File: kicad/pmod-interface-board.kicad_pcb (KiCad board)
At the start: 4 copper layers, 82.9 x 61 mm, 30 parts, among them J1 PMOD Connector 1, J2 PMOD Connector 2, J4 Gameboy Cart Connector, U1 74HCT541, U2 74HCT541, U3 74HC595, U4 74HC595, U5 74HC595, U6 74HC597

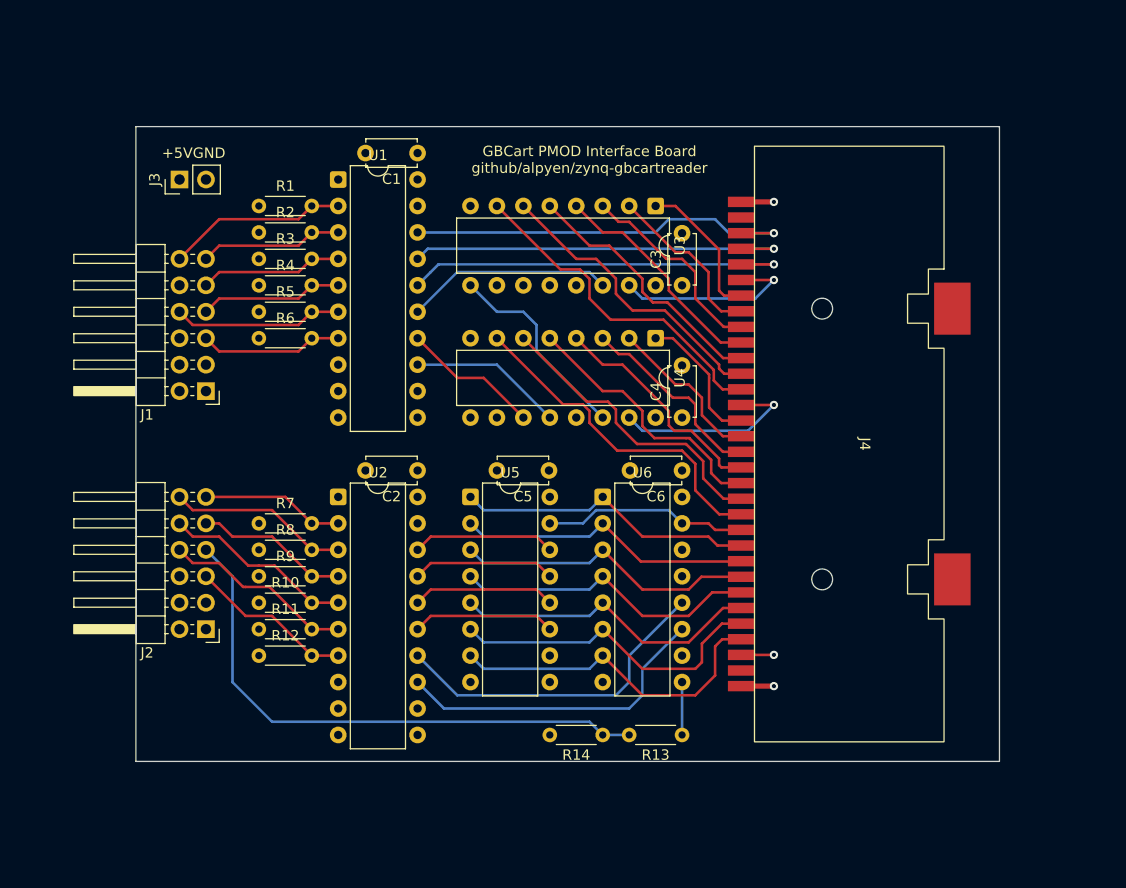
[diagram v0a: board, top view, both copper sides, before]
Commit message: kicad: pcb excess shortened
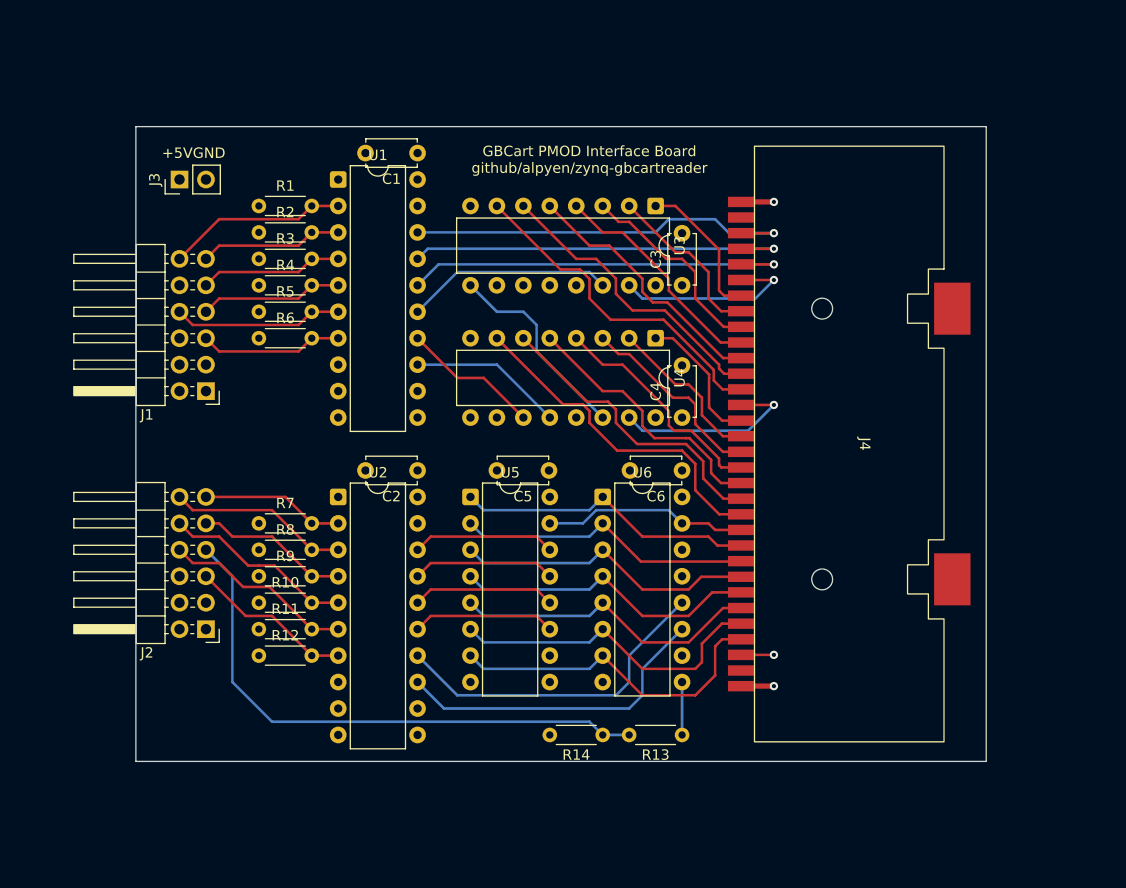
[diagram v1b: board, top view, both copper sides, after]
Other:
- board size 82.9 x 61 mm -> 81.7 x 61 mm
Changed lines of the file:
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@@
 	(gr_rect
 		(start 110.109 60.96)
-		(end 193.04 121.92)
+		(end 191.77 121.92)
 		(stroke
 			(width 0.05)
@@
 	(gr_line
 		(start 96.52 91.44)
-		(end 208.28 91.44)
+		(end 203.2 91.44)
 		(stroke
 			(width 0.15)
@@
 		(polygon
 			(pts
-				(xy 104.14 55.88) (xy 198.12 55.88) (xy 198.12 127) (xy 104.14 127)
+				(xy 104.14 55.88) (xy 196.85 55.88) (xy 196.85 127) (xy 104.14 127)
 			)
 		)
@@
 		(polygon
 			(pts
-				(xy 106.68 58.42) (xy 195.58 58.42) (xy 195.58 124.46) (xy 106.68 124.46)
+				(xy 106.68 58.42) (xy 194.31 58.42) (xy 194.31 124.46) (xy 106.68 124.46)
 			)
 		)

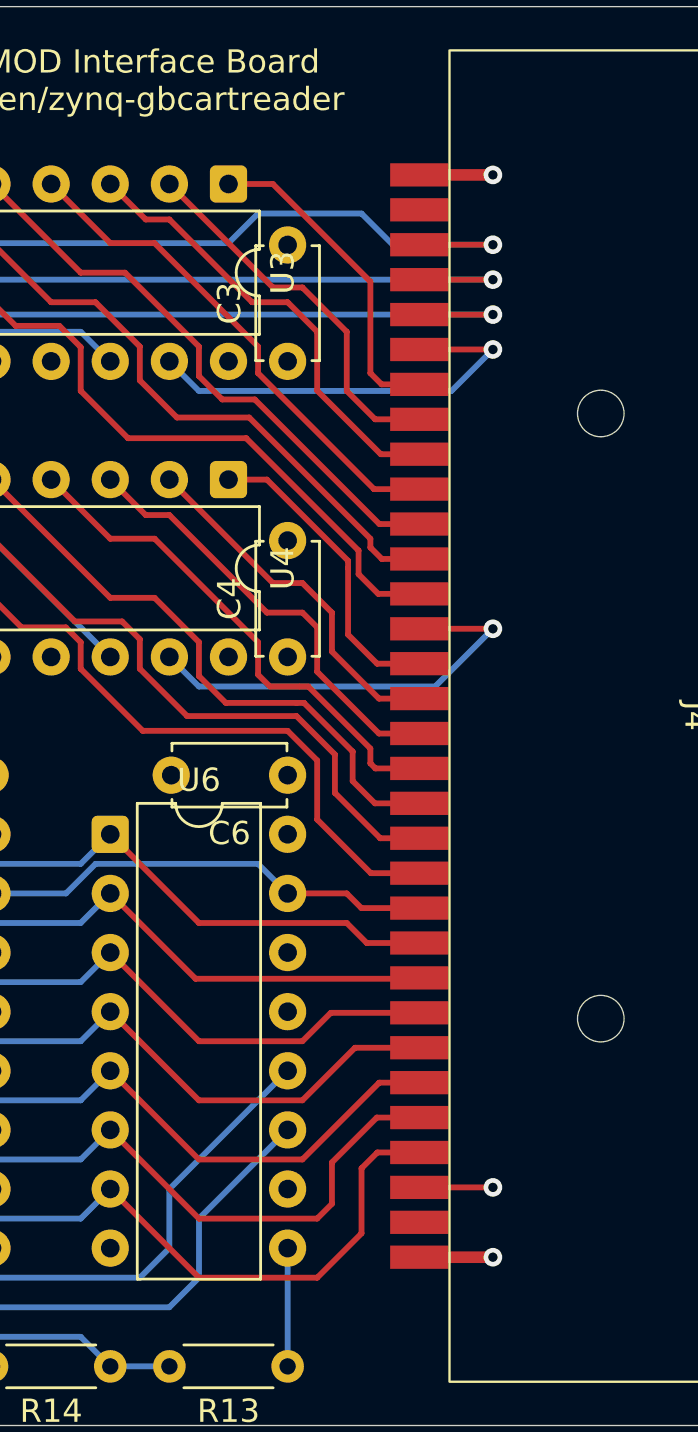
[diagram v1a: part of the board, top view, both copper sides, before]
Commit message: kicad: added copper pour and vias to cart vcc/gnd
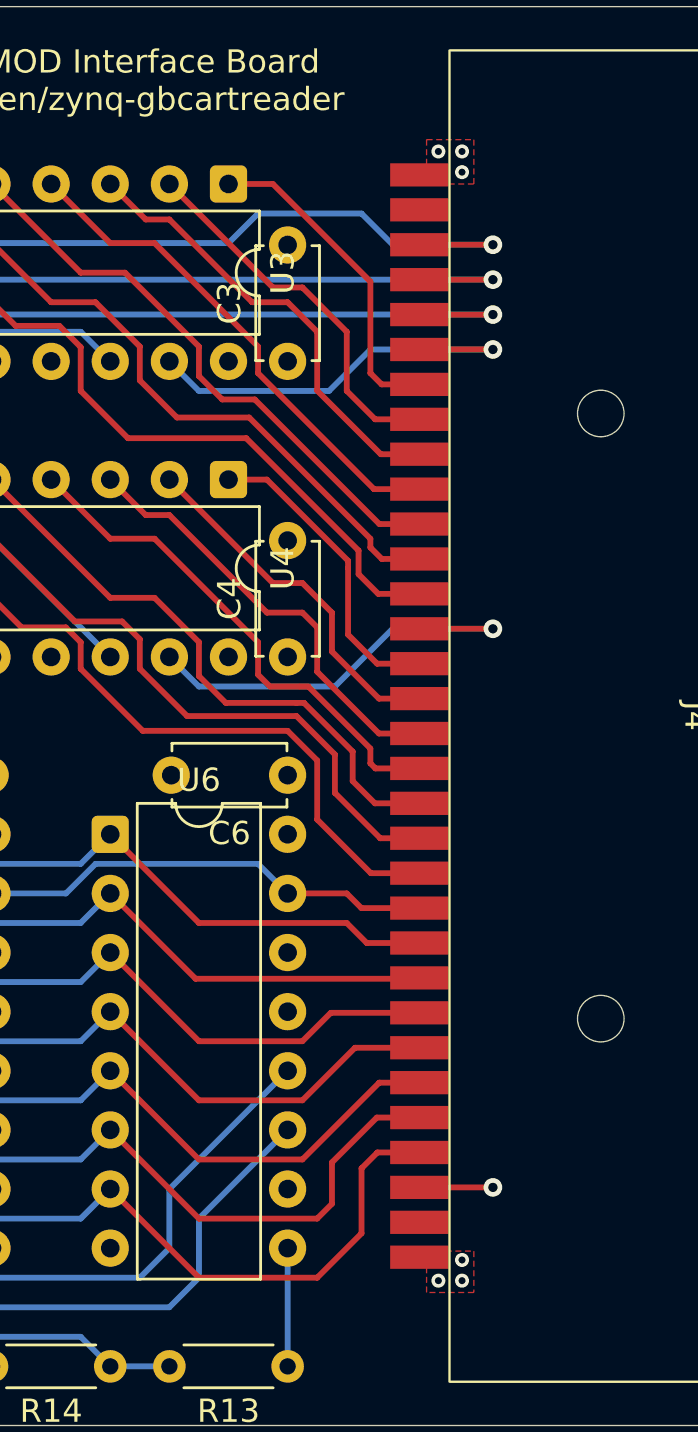
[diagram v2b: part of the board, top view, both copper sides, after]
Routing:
- net GND: track 3.16 -> 0.00 mm, vias 1 -> 3
- net +5V: track 6.33 -> 3.16 mm, vias 2 -> 4
- added copper zone on F.Cu, net +5V
- added copper zone on F.Cu, net GND
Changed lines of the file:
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@@
-	)
-	(segment
-		(start 168.215 68.19)
-		(end 171.38 68.19)
-		(width 0.5)
-		(layer "F.Cu")
-		(net 1)
 	)
 	(segment
@@
 	)
 	(via
-		(at 171.38 68.19)
-		(size 0.8)
-		(drill 0.4)
+		(at 170.053 68.072)
+		(size 0.6)
+		(drill 0.3)
 		(layers "F.Cu" "B.Cu")
+		(free yes)
+		(net 1)
+	)
+	(via
+		(at 169.037 67.183)
+		(size 0.6)
+		(drill 0.3)
+		(layers "F.Cu" "B.Cu")
+		(free yes)
 		(net 1)
 	)
@@
 		(net 1)
 	)
-	(segment
-		(start 168.215 114.69)
-		(end 171.38 114.69)
-		(width 0.5)
-		(layer "F.Cu")
+	(via
+		(at 170.053 67.183)
+		(size 0.6)
+		(drill 0.3)
+		(layers "F.Cu" "B.Cu")
+		(free yes)
+		(net 1)
+	)
+	(via
+		(at 169.037 115.697)
+		(size 0.6)
+		(drill 0.3)
+		(layers "F.Cu" "B.Cu")
+		(free yes)
 		(net 2)
 	)
 	(via
-		(at 171.38 114.69)
-		(size 0.8)
-		(drill 0.4)
+		(at 170.053 114.808)
+		(size 0.6)
+		(drill 0.3)
 		(layers "F.Cu" "B.Cu")
+		(free yes)
+		(net 2)
+	)
+	(via
+		(at 170.053 115.697)
+		(size 0.6)
+		(drill 0.3)
+		(layers "F.Cu" "B.Cu")
+		(free yes)
 		(net 2)
 	)
@@
 	)
 	(segment
-		(start 168.9 90.17)
+		(start 167.072 87.69)
 		(end 171.38 87.69)
 		(width 0.25)
@@
 	)
 	(segment
+		(start 164.592 90.17)
+		(end 167.072 87.69)
+		(width 0.25)
+		(layer "B.Cu")
+		(net 45)
+	)
+	(segment
 		(start 158.75 90.17)
-		(end 168.9 90.17)
+		(end 164.592 90.17)
 		(width 0.25)
 		(layer "B.Cu")
@@
 	)
 	(segment
+		(start 158.75 77.47)
+		(end 164.338 77.47)
+		(width 0.25)
+		(layer "B.Cu")
+		(net 46)
+	)
+	(segment
+		(start 164.338 77.47)
+		(end 166.118 75.69)
+		(width 0.25)
+		(layer "B.Cu")
+		(net 46)
+	)
+	(segment
 		(start 157.48 76.2)
 		(end 158.75 77.47)
@@
 	)
 	(segment
-		(start 169.6 77.47)
+		(start 166.118 75.69)
 		(end 171.38 75.69)
-		(width 0.25)
-		(layer "B.Cu")
-		(net 46)
-	)
-	(segment
-		(start 158.75 77.47)
-		(end 169.6 77.47)
 		(width 0.25)
 		(layer "B.Cu")
@@
 	)
 	(zone
+		(net 1)
+		(net_name "+5V")
+		(layer "F.Cu")
+		(hatch edge 0.5)
+		(priority 3)
+		(connect_pads yes
+			(clearance 0.5)
+		)
+		(min_thickness 0.25)
+		(filled_areas_thickness no)
+		(fill yes
+			(thermal_gap 0.5)
+			(thermal_bridge_width 0.5)
+			(smoothing fillet)
+		)
+		(polygon
+			(pts
+				(xy 168.529 66.675) (xy 170.561 66.675) (xy 170.561 68.58) (xy 168.529 68.58)
+			)
+		)
+	)
+	(zone
+		(net 2)
+		(net_name "GND")
+		(layer "F.Cu")
+		(hatch edge 0.5)
+		(priority 3)
+		(connect_pads yes
+			(clearance 0.5)
+		)
+		(min_thickness 0.25)
+		(filled_areas_thickness no)
+		(fill yes
+			(thermal_gap 0.5)
+			(thermal_bridge_width 0.5)
+			(smoothing fillet)
+		)
+		(polygon
+			(pts
+				(xy 168.529 114.427) (xy 170.561 114.427) (xy 170.561 116.205) (xy 168.529 116.205)
+			)
+		)
+	)
+	(zone

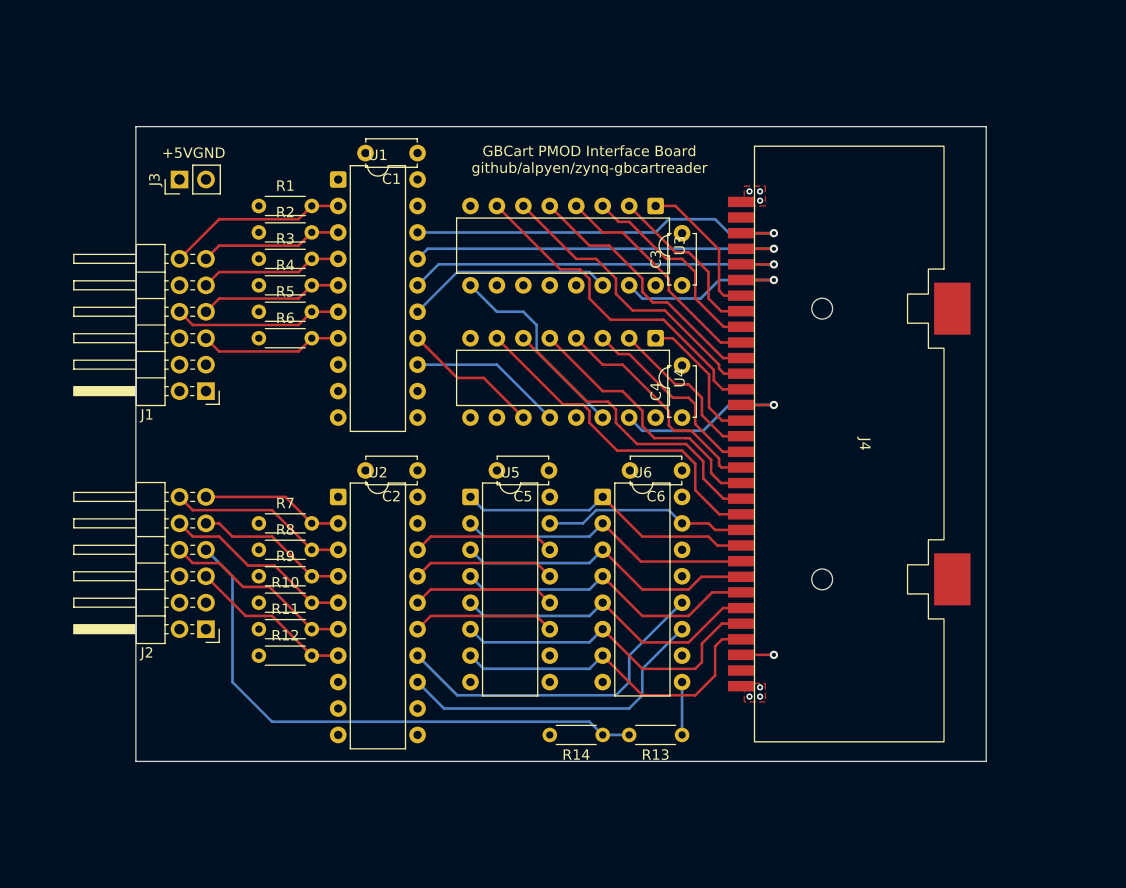
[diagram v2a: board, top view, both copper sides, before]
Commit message: kicad: silkscreen work on the backside
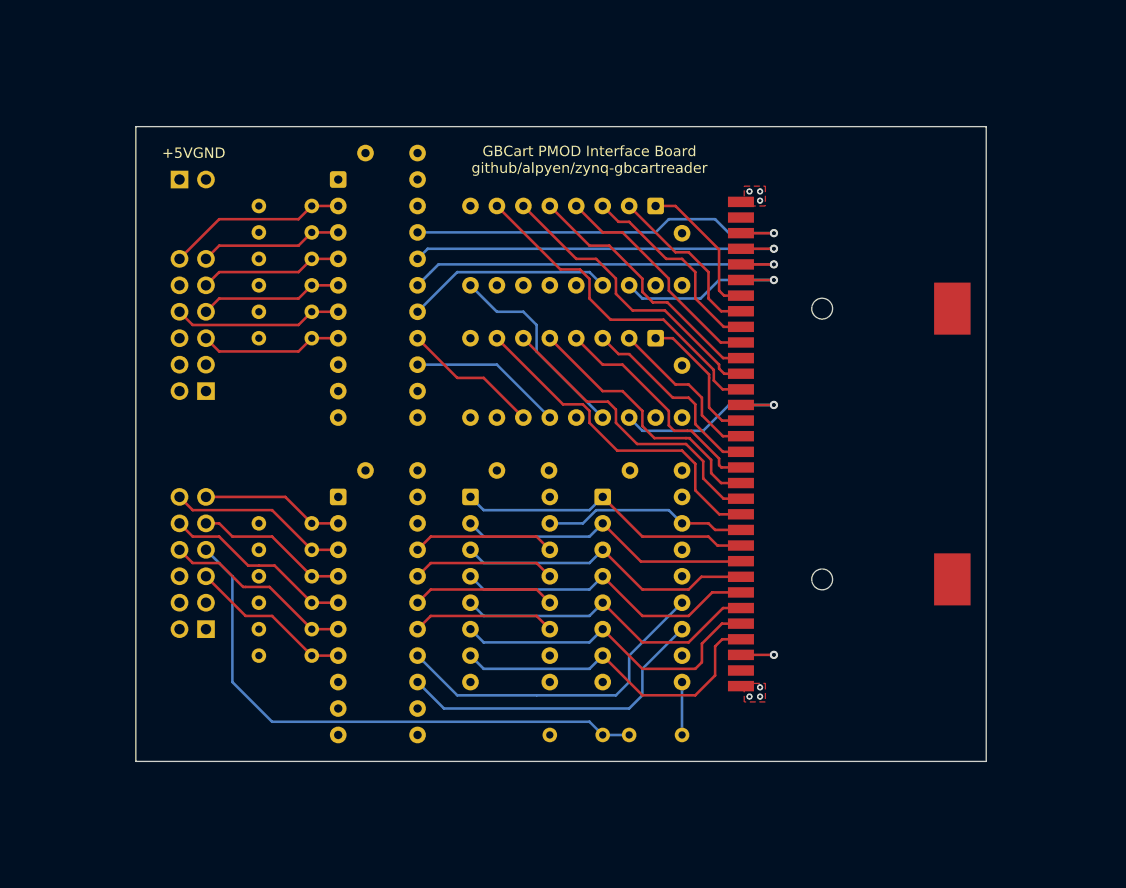
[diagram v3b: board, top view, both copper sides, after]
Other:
- board text added: "100R"
- board text added: "100n"
- board text added: "200R"

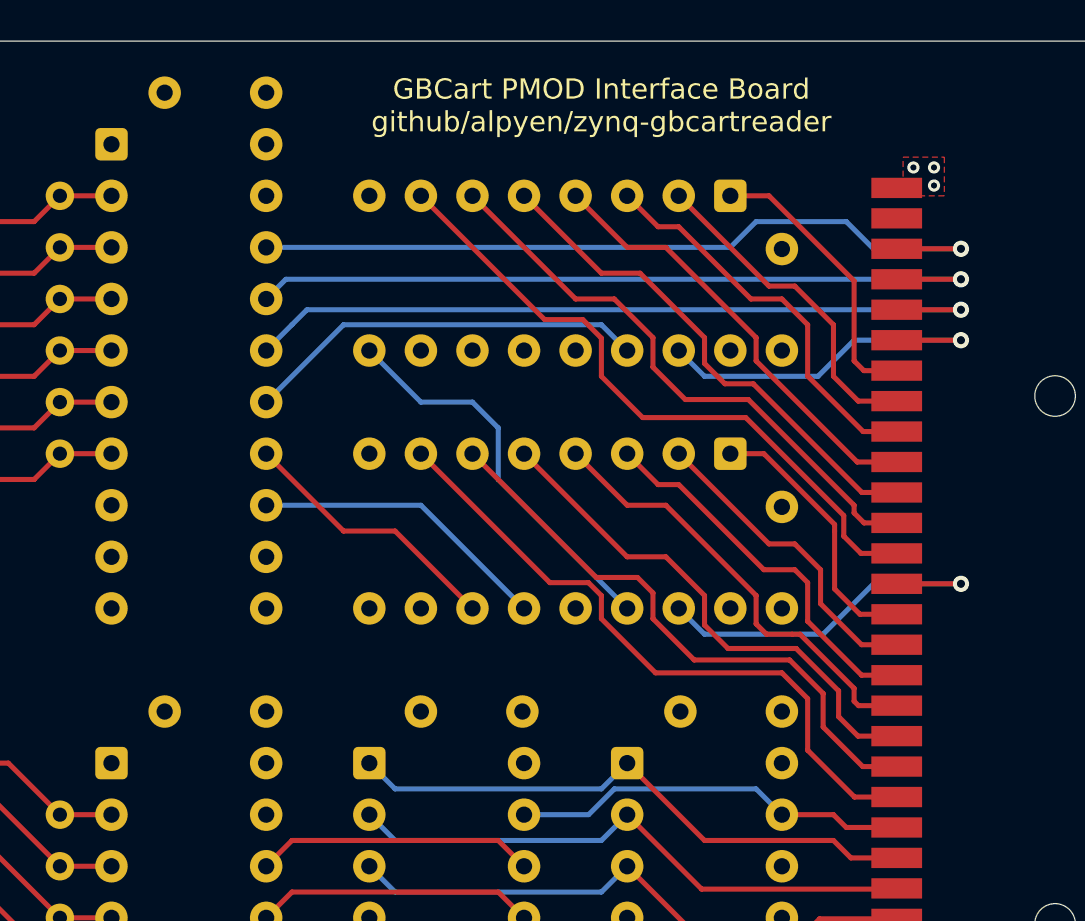
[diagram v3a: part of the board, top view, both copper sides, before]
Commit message: kicad: centered decoupling caps to ics and fixed routing
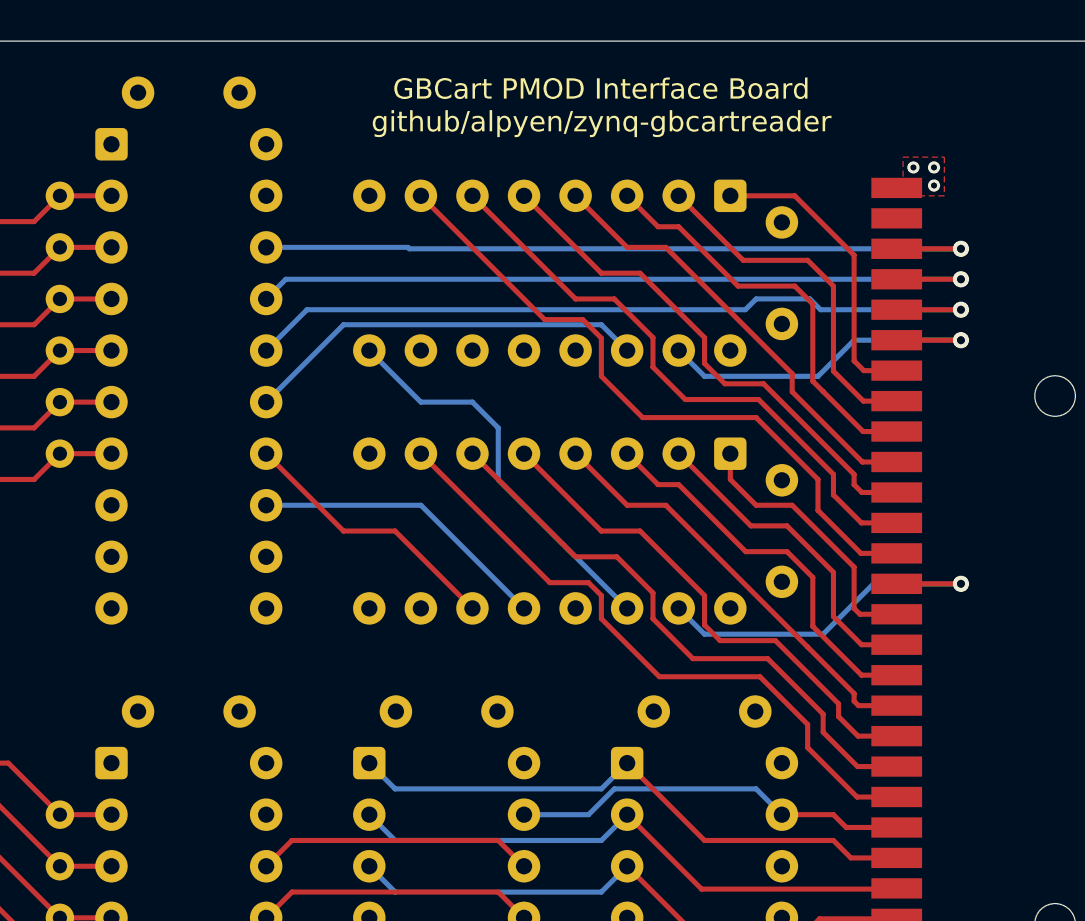
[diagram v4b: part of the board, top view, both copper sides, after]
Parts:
- moved C1 1.31 mm to (135.8, 63.5)
- moved C2 1.31 mm to (135.8, 94.0)
- moved C3 1.31 mm to (162.6, 74.9)
- moved C4 1.31 mm to (162.6, 87.6)
- moved C6 1.31 mm to (161.2, 94.0)
- moved C5 1.23 mm to (148.6, 94.0)
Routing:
- net /~{WR}: track 38.5 -> 37.4 mm
- net /A12: track 22.1 -> 21.2 mm
- net /A2: track 16.4 -> 17.4 mm
- net /A15: track 32.6 -> 31.8 mm
- net /A3: track 19.6 -> 20.3 mm
- net /A1: track 14.1 -> 14.8 mm
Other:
- board text added: "Note: This board is designed to be handsoldered so the cleareance issues can be ignored. The mismatching footprints are due to custom silkscreen."
